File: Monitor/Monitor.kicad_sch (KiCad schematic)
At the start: 26 parts, among them J1 USB_C_Receptacle_USB2.0_14P, SW1 RST, SW2 BOOT, U1 ESP32-S3-WROOM-1, U10 SSD1306, U11 USBLC6-2SC6, U2 AMS1117-3.3, U3 AP2112K-3.0, U4 TMP102xxDRL, U5 LTR-303ALS-01, U6 AHT20, U7 AGS10, U8 BMP388, U9 BQ24075RGT

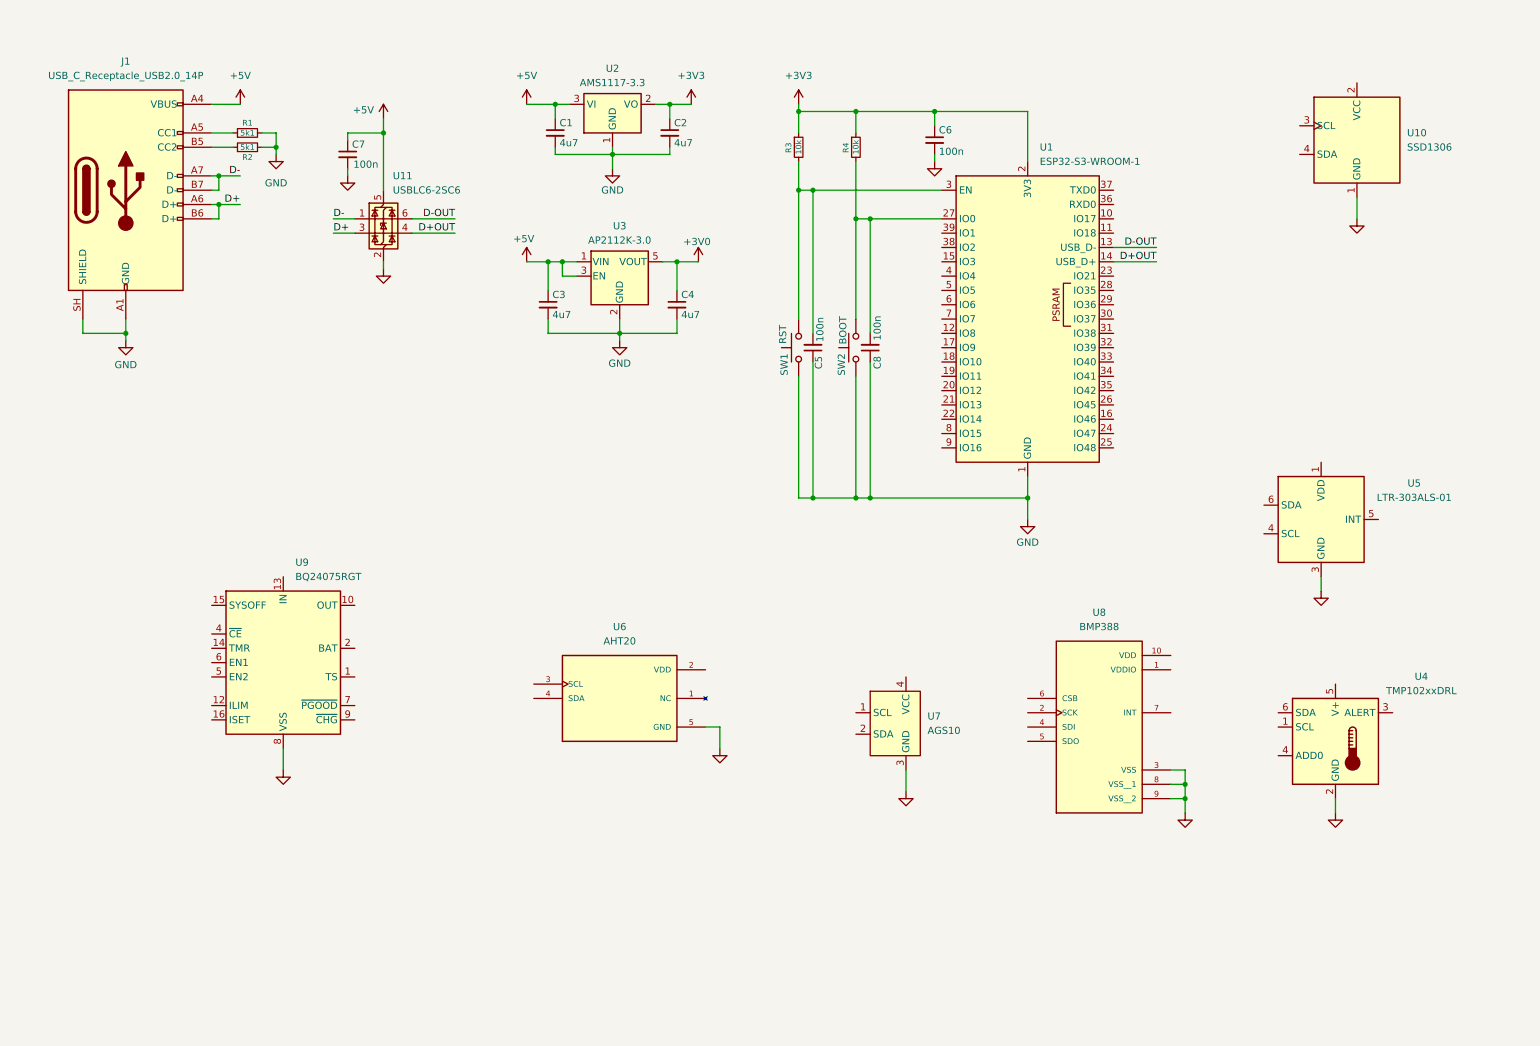
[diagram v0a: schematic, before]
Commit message: Most of Schematic
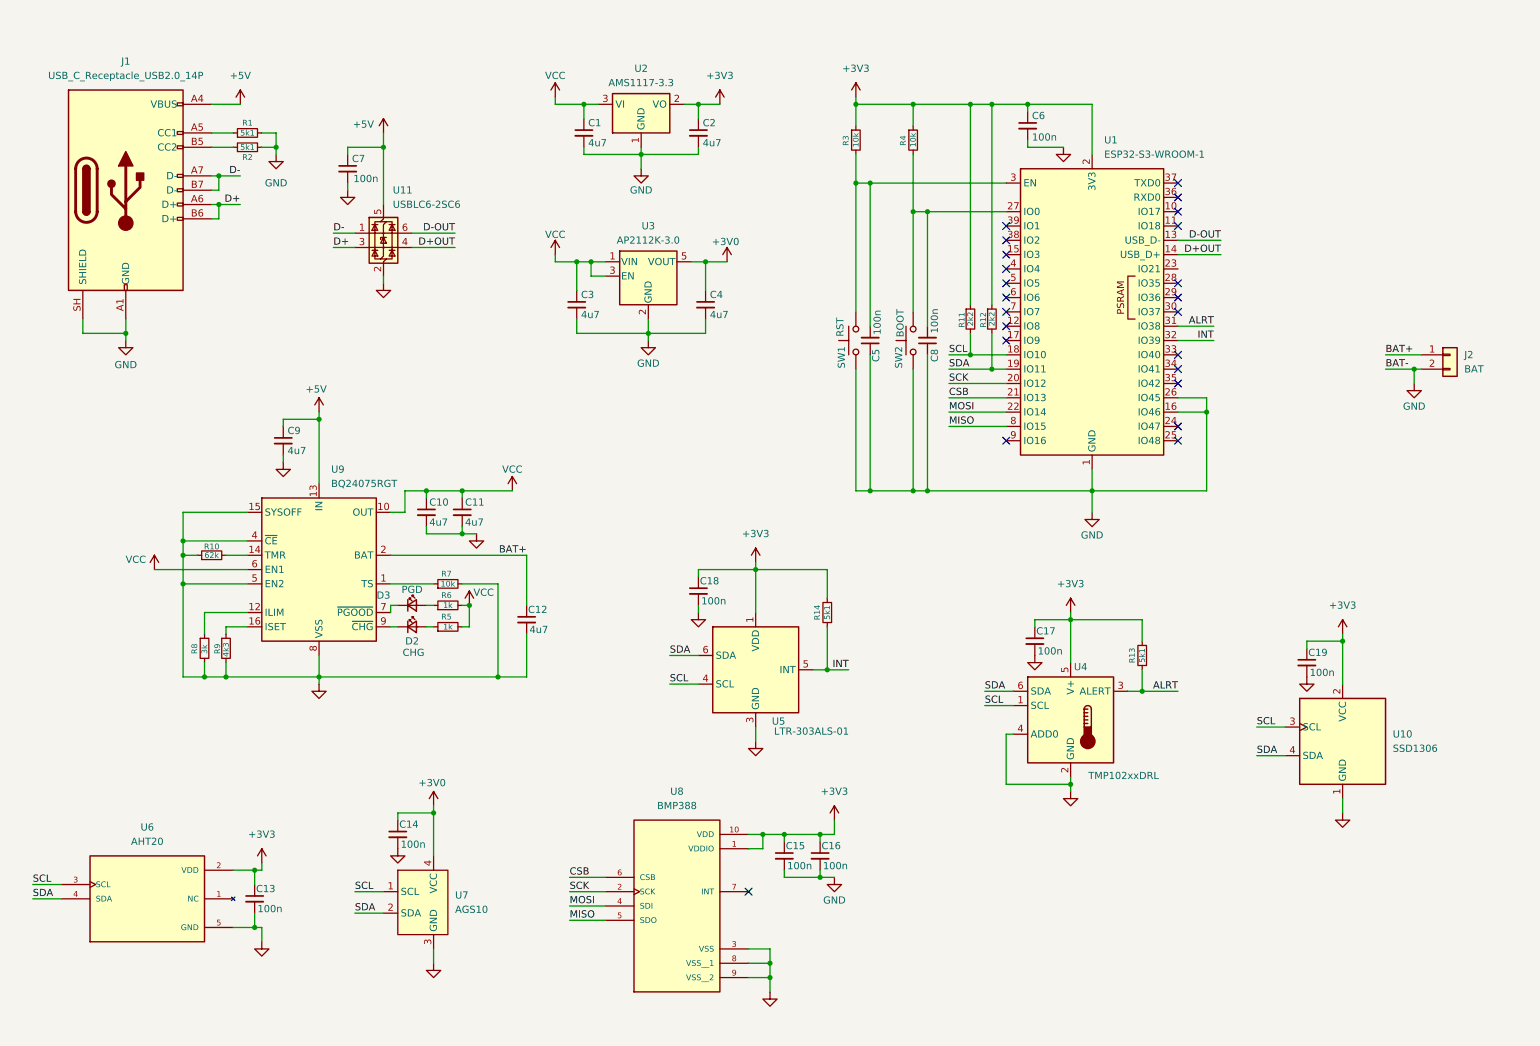
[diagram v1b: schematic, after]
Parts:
- added C10, C11, C12, C9: 4u7, symbol Device:C_Small
- added C13, C14, C15, C16, C17, C18, C19: 100n, symbol Device:C_Small
- added D2: CHG, symbol Device:LED_Small
- added D3: PGD, symbol Device:LED_Small
- added J2: BAT, symbol Connector_Generic:Conn_01x02
- added R10: 62k, symbol Device:R_Small
- added R11, R12: 2k2, symbol Device:R_Small
- added R13, R14: 5k1, symbol Device:R_Small
- added R5, R6: 1k, symbol Device:R_Small
- added R7: 10k, symbol Device:R_Small
- added R8: 3k, symbol Device:R_Small
- added R9: 4k3, symbol Device:R_Small
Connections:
- net +3V0: now also U7.4 (VCC), C14.1
- net +3V3: now also U10.2 (VCC), U4.5 (V+), U5.1 (VDD), U6.2 (VDD), U8.1 (VDDIO), U8.10 (VDD), C13.1, C15.1, C16.1, C17.1, C18.1, C19.1, R11.1, R12.1, R13.2, R14.2
- net +5V: now also U9.13 (IN), C9.1; no longer C1.1, C3.1, U2.3 (VI), U3.1 (VIN), U3.3 (EN)
- net GND: now also U1.16 (IO46), U1.26 (IO45), U4.4 (ADD0), U9.15 (SYSOFF), U9.4 (~{CE}), U9.5 (EN2), C10.2, C11.2, C12.2, C13.2, C14.2, C15.2, C16.2, C17.2, C18.2, C19.2, C9.2, J2.2 (Pin_2), R10.1, R7.2, R8.2, R9.2
- net SCL: now reaches U5.4 (SCL)
- net SCL: now also U1.18 (IO10), U10.3 (SCL), U4.1 (SCL), U6.3 (SCL), U7.1 (SCL), R11.2
- net INT: now reaches U5.5 (INT)
- net INT: now also U1.32 (IO39), R14.1
- net SDA: now reaches U5.6 (SDA)
- net SDA: now also U1.19 (IO11), U10.4 (SDA), U4.6 (SDA), U6.4 (SDA), U7.2 (SDA), R12.2
- net SCK: now reaches U1.20 (IO12)
- net SCK: now also U8.2 (SCK)
- net CSB: now reaches U1.21 (IO13)
- net CSB: now also U8.6 (CSB)
- net MOSI: now reaches U1.22 (IO14)
- net MOSI: now also U8.4 (SDI)
- net ALRT: now reaches U1.31 (IO38)
- net ALRT: now also U4.3 (ALERT), R13.1
- net MISO: now reaches U1.8 (IO15)
- net MISO: now also U8.5 (SDO)
- net at U9.1 (TS): now also R7.1
- net VCC: now reaches U9.10 (OUT), U9.11 (OUT)
- net VCC: now also C1.1, C3.1, U2.3 (VI), U3.1 (VIN), U3.3 (EN), U9.6 (EN1), C10.1, C11.1, R5.2, R6.2
- net at U9.12 (ILIM): now also R8.1
- net at U9.14 (TMR): now also R10.2
- net at U9.16 (ISET): now also R9.1
- net BAT+: now reaches U9.2 (BAT), U9.3 (BAT)
- net BAT+: now also C12.1, J2.1 (Pin_1)
- net at U9.7 (~{PGOOD}): now also D3.1 (K)
- net at U9.9 (~{CHG}): now also D2.1 (K)
- new net: D2.2 (A), R5.1
- new net: D3.2 (A), R6.1
- no-connect marks 0 -> 23
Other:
- moved on the sheet: C1, C2, C3, C4, C5, C6, C7, C8, R3, R4, SW1, SW2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

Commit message: Finish PCB + pictures + BOM
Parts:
- removed C16: 100n, symbol Device:C_Small
- removed U2: AMS1117-3.3, Package_TO_SOT_SMD:SOT-223-3_TabPin2, symbol Regulator_Linear:AMS1117-3.3
- added U5: AMS1117-3.3, Package_TO_SOT_SMD:SOT-223-3_TabPin2, symbol Regulator_Linear:AMS1117-3.3
- C1: renamed from C14; footprint (none) -> Capacitor_SMD:C_0603_1608Metric
- C10: renamed from C2; footprint (none) -> Capacitor_SMD:C_0603_1608Metric
- C11: renamed from C4; footprint (none) -> Capacitor_SMD:C_0603_1608Metric
- C12: renamed from C18; footprint (none) -> Capacitor_SMD:C_0603_1608Metric
- C13: renamed from C5; footprint (none) -> Capacitor_SMD:C_0603_1608Metric
- C14: renamed from C13; footprint (none) -> Capacitor_SMD:C_0603_1608Metric
- C15: renamed from C8; footprint (none) -> Capacitor_SMD:C_0603_1608Metric
- C16: renamed from C6; footprint (none) -> Capacitor_SMD:C_0603_1608Metric
- C17: footprint (none) -> Capacitor_SMD:C_0603_1608Metric
- C18: renamed from C19; footprint (none) -> Capacitor_SMD:C_0603_1608Metric
- C2: renamed from C9; footprint (none) -> Capacitor_SMD:C_0603_1608Metric
- C3: renamed from C10; footprint (none) -> Capacitor_SMD:C_0603_1608Metric
- C4: renamed from C7; footprint (none) -> Capacitor_SMD:C_0603_1608Metric
- C5: renamed from C11; footprint (none) -> Capacitor_SMD:C_0603_1608Metric
- C6: renamed from C12; footprint (none) -> Capacitor_SMD:C_0603_1608Metric
- C7: renamed from C15; footprint (none) -> Capacitor_SMD:C_0603_1608Metric
- C8: renamed from C3; footprint (none) -> Capacitor_SMD:C_0603_1608Metric
- C9: renamed from C1; footprint (none) -> Capacitor_SMD:C_0603_1608Metric
- D1: renamed from D3; footprint (none) -> LED_SMD:LED_1206_3216Metric
- D2: footprint (none) -> LED_SMD:LED_1206_3216Metric
- J1: footprint (none) -> Connector_USB:USB_C_Receptacle_G-Switch_GT-USB-7010ASV
- J2: footprint (none) -> Connector_JST:JST_PH_B2B-PH-K_1x02_P2.00mm_Vertical
- R1: renamed from R8; footprint (none) -> Resistor_SMD:R_0603_1608Metric
- R10: renamed from R3; footprint (none) -> Resistor_SMD:R_0603_1608Metric
- R11: renamed from R4; footprint (none) -> Resistor_SMD:R_0603_1608Metric
- R12: renamed from R11; footprint (none) -> Resistor_SMD:R_0603_1608Metric
- R13: renamed from R12; footprint (none) -> Resistor_SMD:R_0603_1608Metric
- R14: renamed from R13; footprint (none) -> Resistor_SMD:R_0603_1608Metric
- R2: renamed from R10; footprint (none) -> Resistor_SMD:R_0603_1608Metric
- R3: renamed from R9; footprint (none) -> Resistor_SMD:R_0603_1608Metric
- R4: renamed from R1; footprint (none) -> Resistor_SMD:R_0603_1608Metric
- R5: renamed from R2; footprint (none) -> Resistor_SMD:R_0603_1608Metric
- R6: renamed from R7; footprint (none) -> Resistor_SMD:R_0603_1608Metric
- R7: renamed from R6; footprint (none) -> Resistor_SMD:R_0603_1608Metric
- R8: renamed from R5; footprint (none) -> Resistor_SMD:R_0603_1608Metric
- R9: renamed from R14; footprint (none) -> Resistor_SMD:R_0603_1608Metric
- SW1, SW2: footprint (none) -> Button_Switch_SMD:SW_SPST_PTS647_Sx38
- renumbered U7 to U1, U1 to U10, U10 to U11, U9 to U2, U11 to U3, U8 to U4, U3 to U6, U5 to U7, U6 to U8, U4 to U9
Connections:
- net +3V3: now also R7.2, R8.2, U5.2 (VO)
- net GND: now also U5.1 (GND)
- net MISO: now also U10.22 (IO14); no longer U10.8 (IO15)
- net MOSI: now also U10.23 (IO21); no longer U10.22 (IO14)
- net SCL: now also U10.17 (IO9); no longer U10.18 (IO10)
- net SDA: now also U10.18 (IO10); no longer U10.19 (IO11)
- net VCC: now also U5.3 (VI); no longer R7.2, R8.2
- net D+OUT renamed DOut+
- net D-OUT renamed DOut-
- no-connect marks 23 -> 24
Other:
- note added: "Air Pressure"
- note added: "Air Quality"
- note added: "BATTERY"
- note added: "ESP32"
- note added: "Humidity/Moisture"
- note added: "Light"
- note added: "POWER"
- note added: "Screen"
- note added: "Temperature"
- moved on the sheet: C1, C11, C12, C13, C14, C15, C16, C17, C18, C2, C3, C4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
